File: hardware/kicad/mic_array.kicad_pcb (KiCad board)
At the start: 2 copper layers, 84 x 84 mm, 37 parts, among them J1 CLK D1-D8 3V3 GND GND, U1 SPH0641LU4H-1 PLACEHOLDER, U10 SPH0641LU4H-1 PLACEHOLDER, U11 SPH0641LU4H-1 PLACEHOLDER, U12 SPH0641LU4H-1 PLACEHOLDER, U13 SPH0641LU4H-1 PLACEHOLDER, U14 SPH0641LU4H-1 PLACEHOLDER, U15 SPH0641LU4H-1 PLACEHOLDER, U16 SPH0641LU4H-1 PLACEHOLDER, U2 SPH0641LU4H-1 PLACEHOLDER, U3 SPH0641LU4H-1 PLACEHOLDER, U4 SPH0641LU4H-1 PLACEHOLDER, U5 SPH0641LU4H-1 PLACEHOLDER, U6 SPH0641LU4H-1 PLACEHOLDER, U7 SPH0641LU4H-1 PLACEHOLDER, U8 SPH0641LU4H-1 PLACEHOLDER, U9 SPH0641LU4H-1 PLACEHOLDER

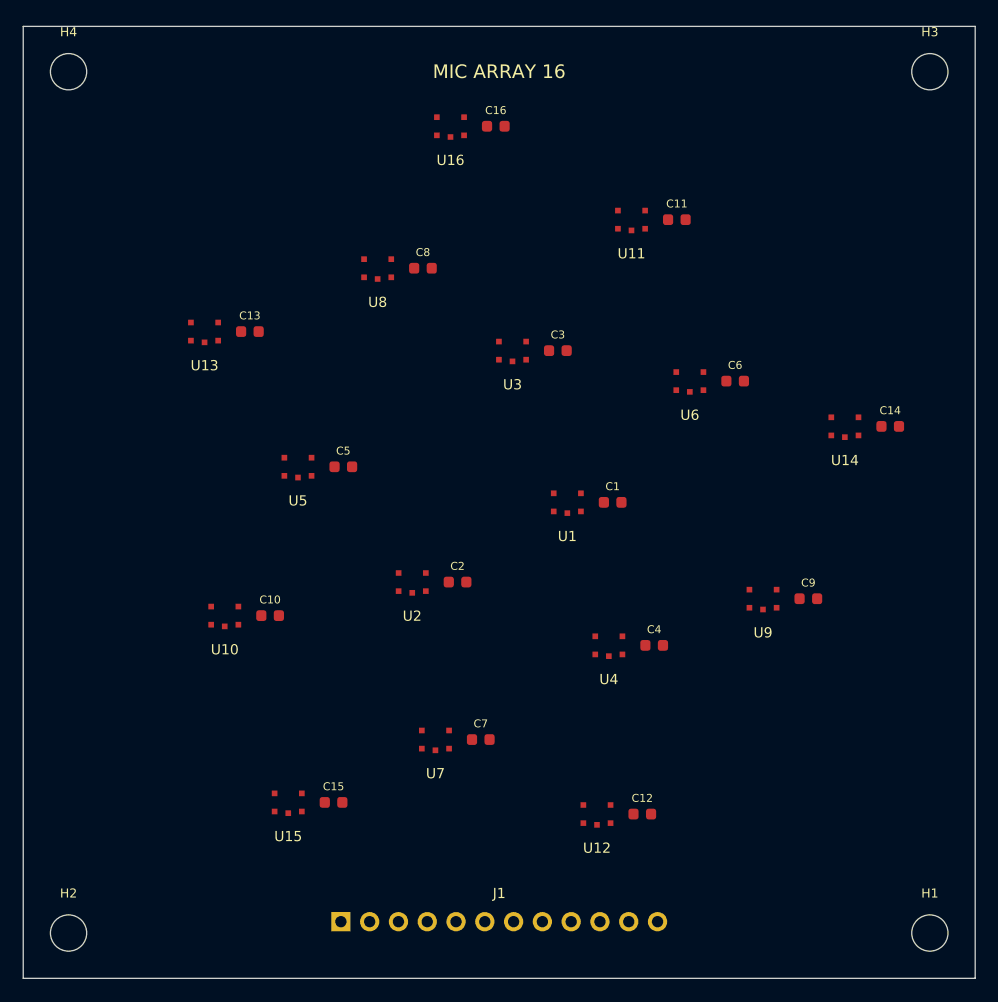
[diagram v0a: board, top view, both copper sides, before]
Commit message: Add PCB design checks, TX keepout and courtyards; move spiral to r = 8.5*sqrt(i+1)
The checks found that U1 sat under the transmitter in the board centre.
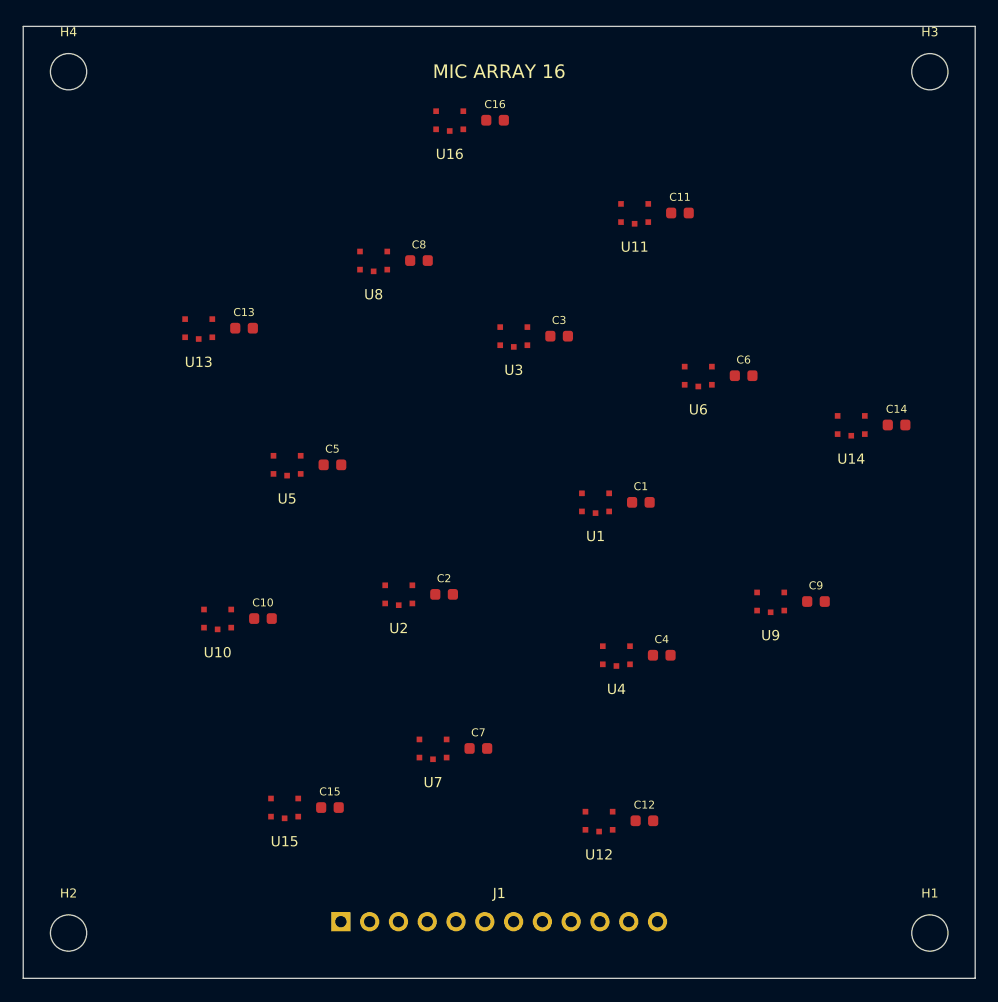
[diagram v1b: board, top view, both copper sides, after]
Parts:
- moved C1 2.49 mm to (112.5, 100.0)
- moved U1 2.49 mm to (108.5, 100.0)
- moved C2 1.61 mm to (95.1, 108.1)
- moved U2 1.61 mm to (91.1, 108.1)
- moved C3 1.28 mm to (105.3, 85.3)
- moved U3 1.28 mm to (101.3, 85.3)
- moved C4 1.10 mm to (114.3, 113.5)
- moved U4 1.10 mm to (110.3, 113.5)
- moved C5 0.97 mm to (85.3, 96.7)
- moved U5 0.97 mm to (81.3, 96.7)
- moved C6 0.89 mm to (121.6, 88.8)
- moved U6 0.89 mm to (117.6, 88.8)
- moved C7 0.82 mm to (98.2, 121.7)
- moved U7 0.82 mm to (94.2, 121.7)
- moved C8 0.76 mm to (92.9, 78.7)
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
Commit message: Use real SPH0641 footprint with acoustic port hole; add 2-mic test board
Footprint is KiCad's Sensor_Audio:Knowles_LGA-5_3.5x2.65mm. The footprint is placed so the
acoustic port, 0.77 mm from the package centre, sits on the placement point.
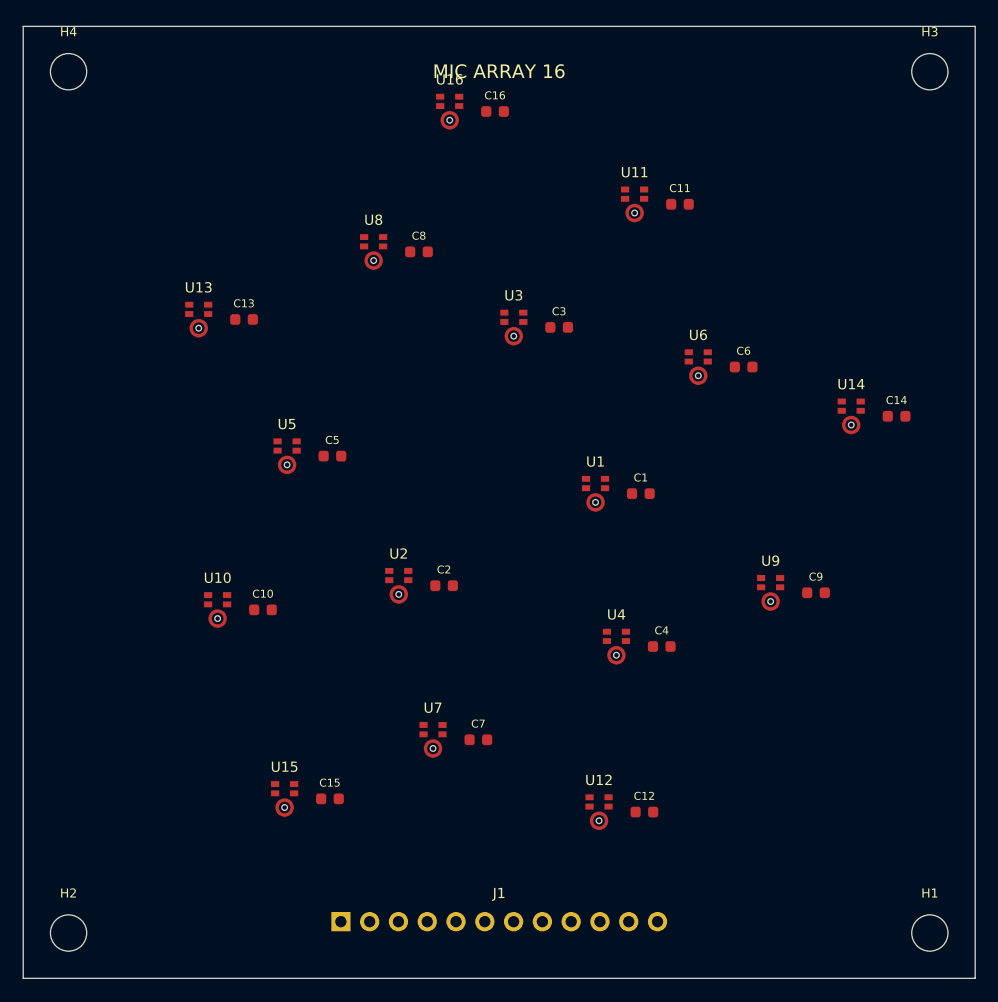
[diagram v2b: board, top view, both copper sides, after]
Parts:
- U1, U10, U11, U12, U13, U14, U15, U16, U2, U3, U4, U5, U6, U7, U8, U9: value SPH0641LU4H-1 PLACEHOLDER -> SPH0641LU4H-1; footprint PLACEHOLDER:SPH0641LU4H-1 -> Sensor_Audio:Knowles_LGA-5_3.5x2.65mm
- moved C12 0.77 mm to (112.8, 127.3)
- moved C13 0.77 mm to (77.5, 83.9)
- moved C15 0.77 mm to (85.1, 126.2)
- moved C2 0.77 mm to (95.1, 107.3)
- moved C3 0.77 mm to (105.3, 84.6)
- moved C7 0.77 mm to (98.2, 120.9)
- moved C9 0.77 mm to (128.0, 108.0)
- moved U12 0.77 mm to (108.8, 127.3)
- moved U13 0.77 mm to (73.5, 83.9)
- moved U15 0.77 mm to (81.1, 126.2)
- moved U2 0.77 mm to (91.1, 107.3)
- moved U3 0.77 mm to (101.3, 84.6)
- moved U7 0.77 mm to (94.2, 120.9)
- moved U9 0.77 mm to (124.0, 108.0)
- moved C1 0.77 mm to (112.5, 99.2)
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
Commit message: Byt sändare till CUSA-T75-18-2400-TH: större keepout och spiral utflyttad (#4)
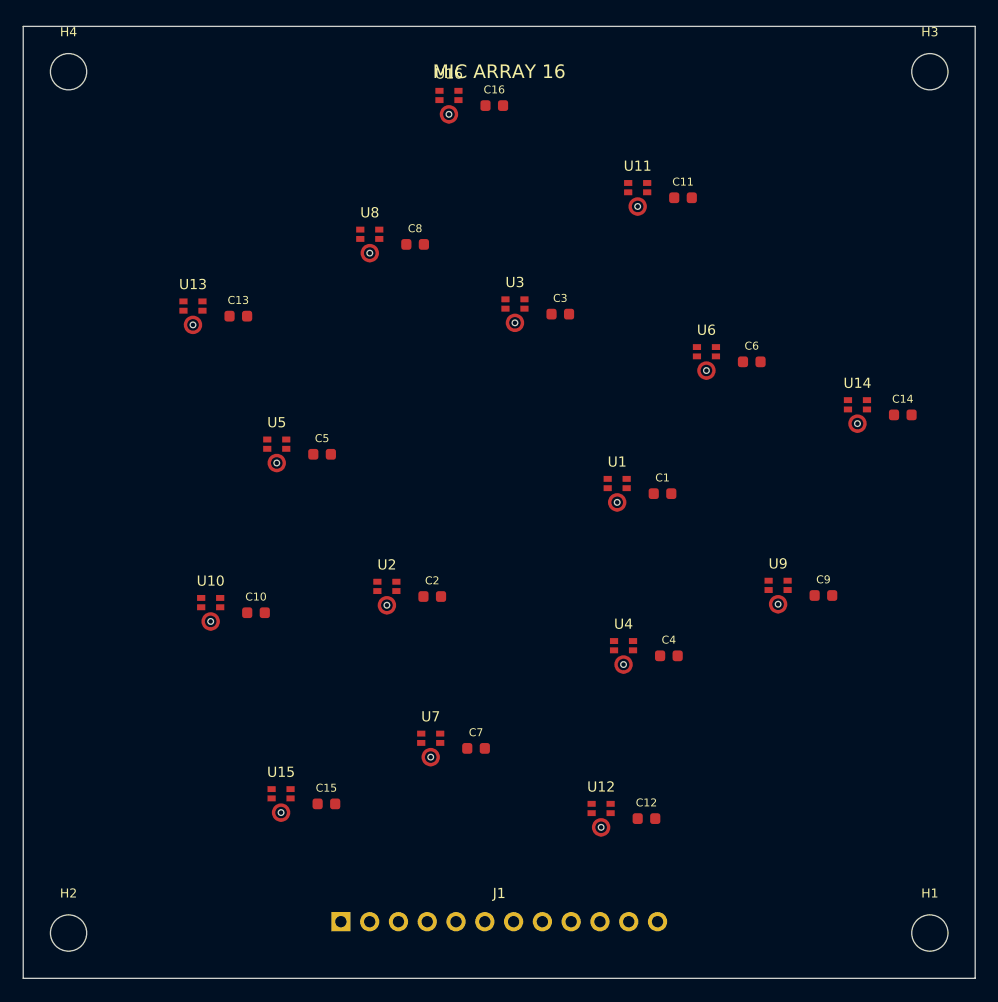
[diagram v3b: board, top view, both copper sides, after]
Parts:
- moved C1 1.91 mm to (114.4, 99.2)
- moved U1 1.91 mm to (110.4, 99.2)
- moved C2 1.42 mm to (94.1, 108.3)
- moved U2 1.42 mm to (90.1, 108.3)
- moved C3 1.18 mm to (105.4, 83.4)
- moved U3 1.18 mm to (101.4, 83.4)
- moved C4 1.03 mm to (115.0, 113.5)
- moved U4 1.03 mm to (111.0, 113.5)
- moved C5 0.93 mm to (84.4, 95.8)
- moved U5 0.93 mm to (80.4, 95.8)
- moved C6 0.85 mm to (122.3, 87.6)
- moved U6 0.85 mm to (118.3, 87.6)
- moved C7 0.79 mm to (98.0, 121.7)
- moved U7 0.79 mm to (94.0, 121.7)
- moved C8 0.74 mm to (92.6, 77.2)
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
